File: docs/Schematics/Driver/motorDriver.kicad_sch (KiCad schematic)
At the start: 2 parts

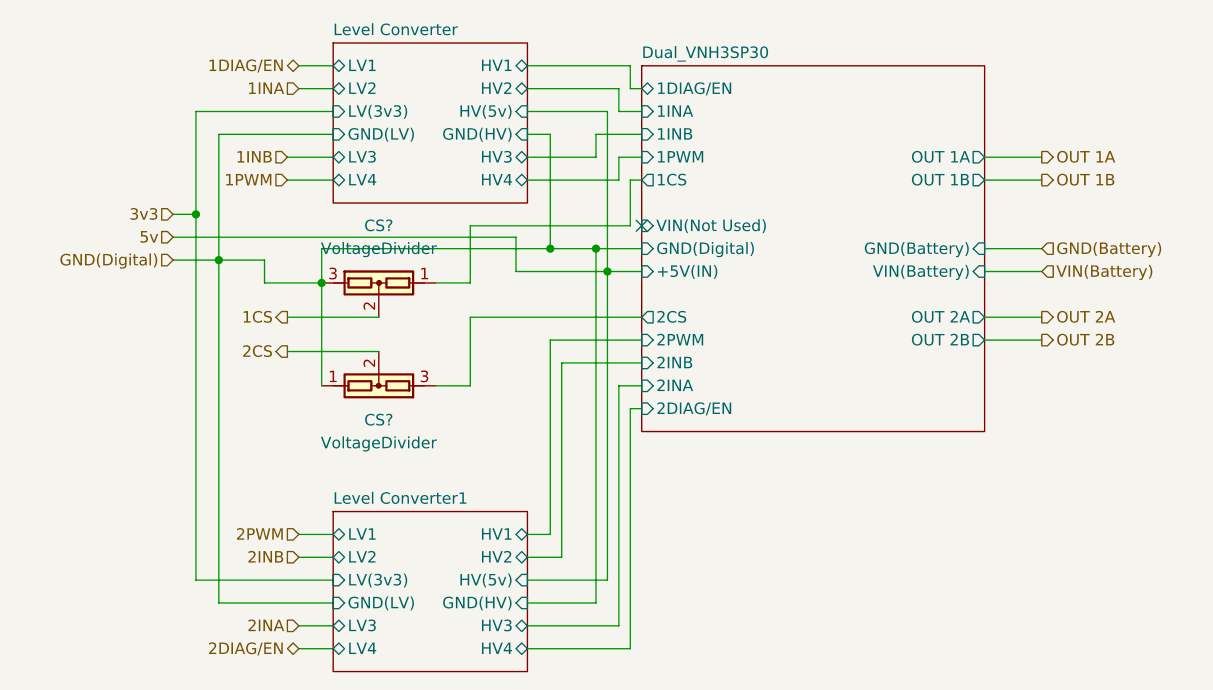
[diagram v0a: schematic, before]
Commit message: First scematic design for the card
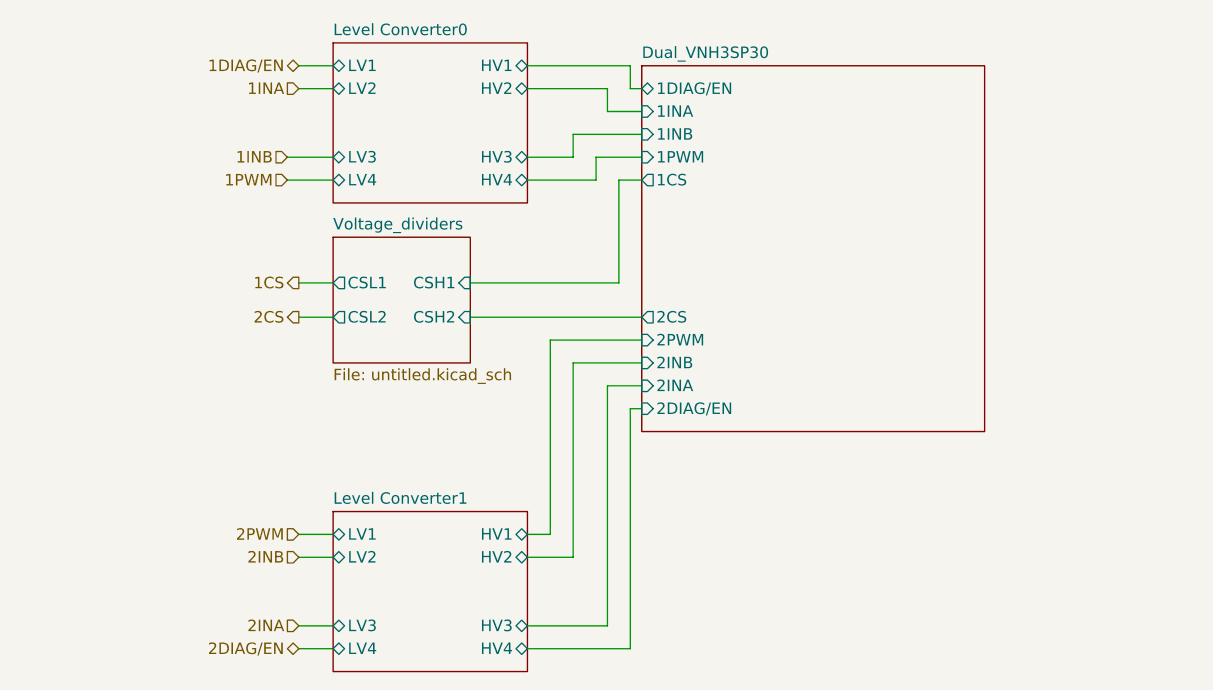
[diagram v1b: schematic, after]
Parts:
- removed CS? (x2): VoltageDivider, symbol Device:VoltageDivider
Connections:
- no-connect marks 1 -> 0
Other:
- sheet Level Converter renamed Level Converter0
- added sheet Voltage_dividers (untitled.kicad_sch)
- sheet Dual_VNH3SP30 ports: added none; removed +5V(IN), GND(Battery), GND(Digital), OUT 1A, OUT 1B, OUT 2A, OUT 2B, VIN(Battery), VIN(Not Used)
- sheet Level Converter0 ports: added none; removed GND(HV), GND(LV), HV(5v), LV(3v3)
- sheet Level Converter1 ports: added none; removed GND(HV), GND(LV), HV(5v), LV(3v3)
- company: (none) -> HiQ
- title: (none) -> Arty Z7 IO expander card

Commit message: First version of the routed board is done
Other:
- title: Arty Z7 IO expander card -> Arty Z7 IO Board
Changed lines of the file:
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@@
   (paper "A4")
   (title_block
-    (title "Arty Z7 IO expander card")
+    (title "Arty Z7 IO Board")
     (date "2022-12-24")
-    (rev "0.1")
+    (rev "${VER}")
     (company "HiQ")
   )
